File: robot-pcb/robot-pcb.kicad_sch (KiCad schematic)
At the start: 47 parts, among them J1 Conn_02x03_Odd_Even, J2 Conn_01x05_Female, J3 Conn_02x05_Odd_Even, J4 Conn_01x03_Male, J5 Conn_01x03_Male, J6 Screw_Terminal_01x02, J7 Screw_Terminal_01x02, J8 Screw_Terminal_01x02, J9 Screw_Terminal_01x02, SW1 SW_Push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

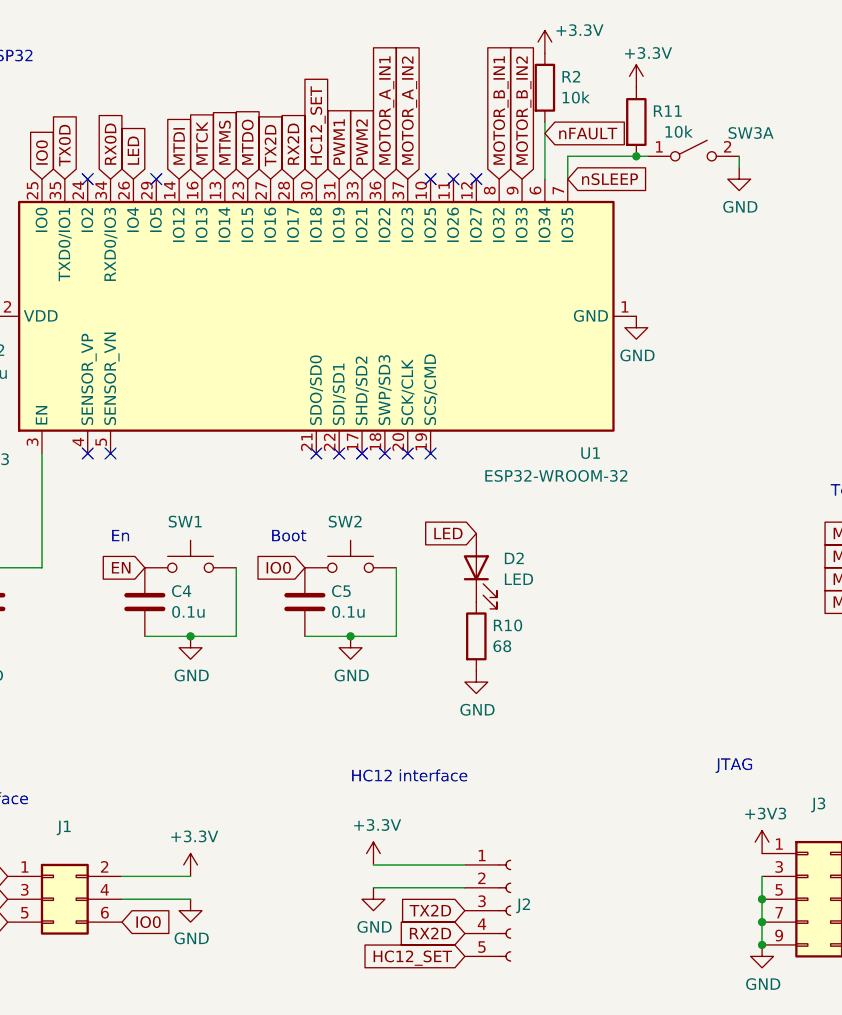
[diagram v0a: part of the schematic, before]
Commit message: Update KiCad version
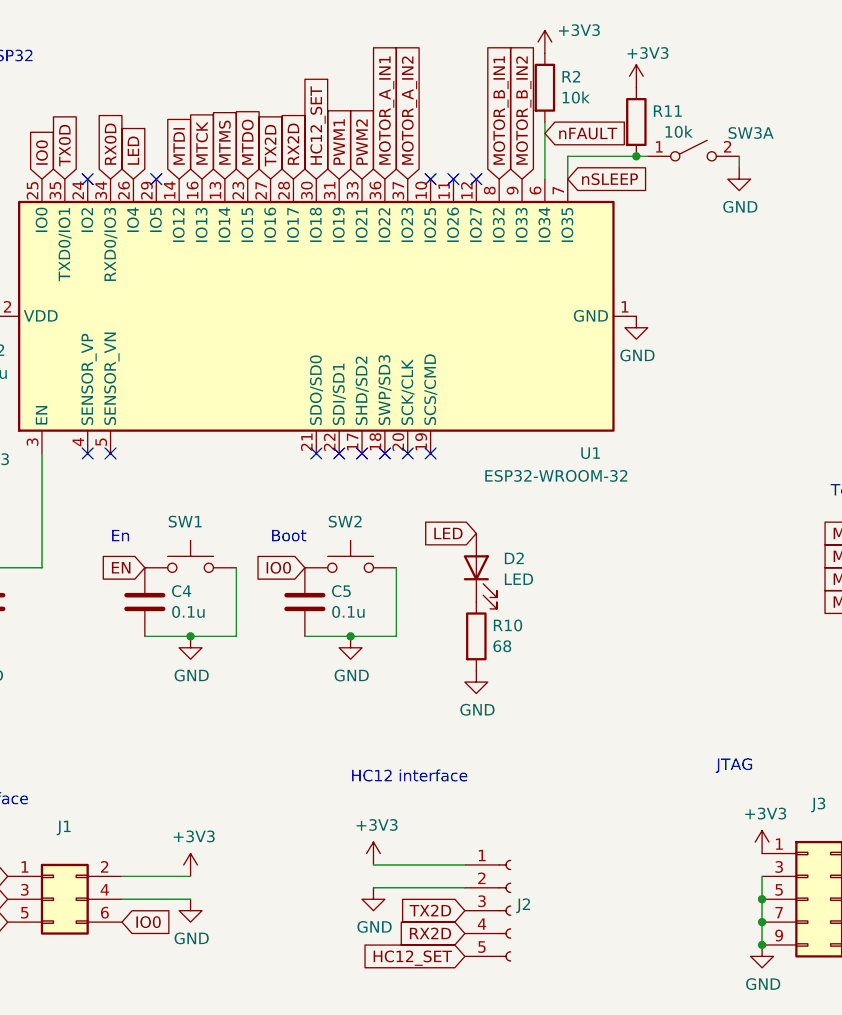
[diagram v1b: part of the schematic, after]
